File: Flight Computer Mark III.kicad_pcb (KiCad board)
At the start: 4 copper layers, 88.2 x 58.8 mm, 69 parts, among them J1 Conn_01x02, J2 USB_C_Receptacle_USB2.0_16P, Q1 PSMN075-100MSE, Q2 PSMN075-100MSE, Q3 PSMN075-100MSE, U1 CP2102N-Axx-xQFN20

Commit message: lol
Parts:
- moved 3.3VREG1 26.8 mm to (216.8, 127.4)
- moved C4 26.8 mm to (216.0, 124.3)
- moved I1 26.8 mm to (216.8, 133.4)
- moved R1 26.8 mm to (219.2, 124.9)
- moved C5 26.8 mm to (219.8, 137.1)
- moved C6 26.8 mm to (213.9, 137.1)
- moved R2 26.8 mm to (216.8, 122.6)
- moved C1 26.8 mm to (219.2, 128.1)
- moved DWNLD1 23.0 mm to (173.4, 67.0)
- moved R10 22.9 mm to (166.9, 86.3), turned to -90 degrees
- moved R13 22.5 mm to (162.0, 78.5)
- moved C11 22.4 mm to (171.0, 91.1)
- moved J2 22.4 mm to (167.8, 80.2)
- moved R11 22.4 mm to (169.1, 86.3)
- moved R18 22.4 mm to (174.1, 91.8)
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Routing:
- net MOSI_SPI0: track 8.58 -> 50.2 mm, vias 1 -> 2
- net Servo3: track 59.2 -> 22.3 mm
- net CS_SPI0: track 8.00 -> 32.6 mm, vias 0 -> 1
- net MISO_SPI0: track 21.1 -> 39.0 mm
- net TXtoURX: track 17.8 -> 30.8 mm, vias 0 -> 2
- net RXtoUTX: track 17.7 -> 28.2 mm, vias 0 -> 2
- net CLK_SPI0: track 18.7 -> 13.7 mm
- net CS_Magnetometer: track 35.5 -> 32.6 mm
- net Servo2: track 17.4 -> 19.0 mm
- net CLK_IMU: track 20.4 -> 19.0 mm
- net Servo1: track 13.2 -> 14.1 mm, vias 0 -> 1
- net GND: track 17.6 -> 16.8 mm, vias 42 -> 38

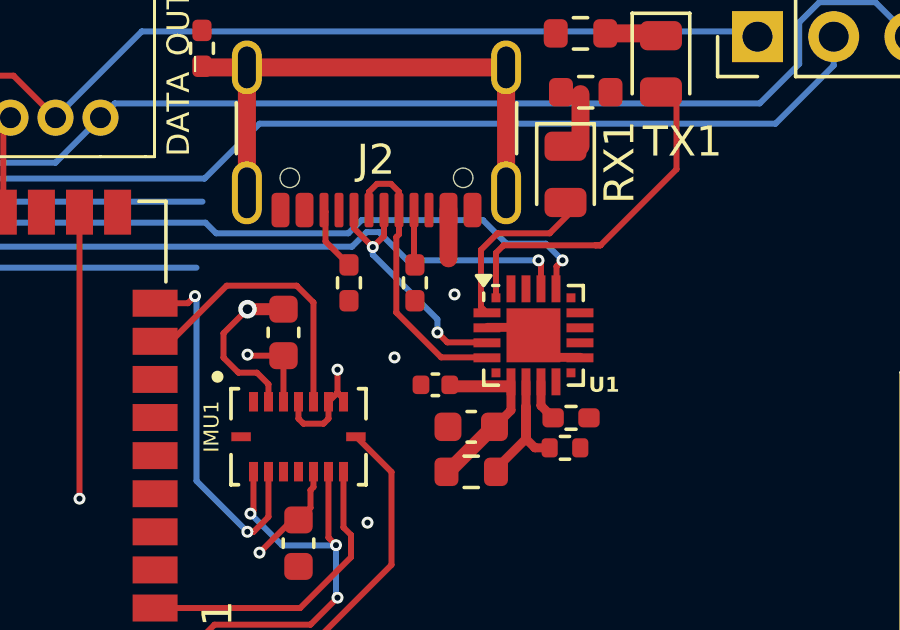
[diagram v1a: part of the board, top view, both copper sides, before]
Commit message: Added 3d models
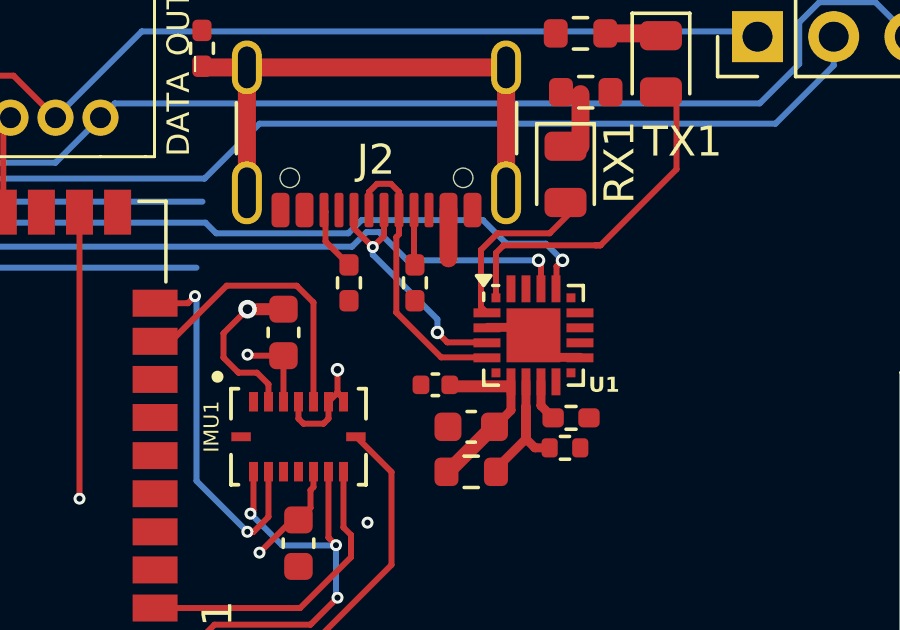
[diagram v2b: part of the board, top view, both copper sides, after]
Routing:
- net GND: vias 38 -> 36

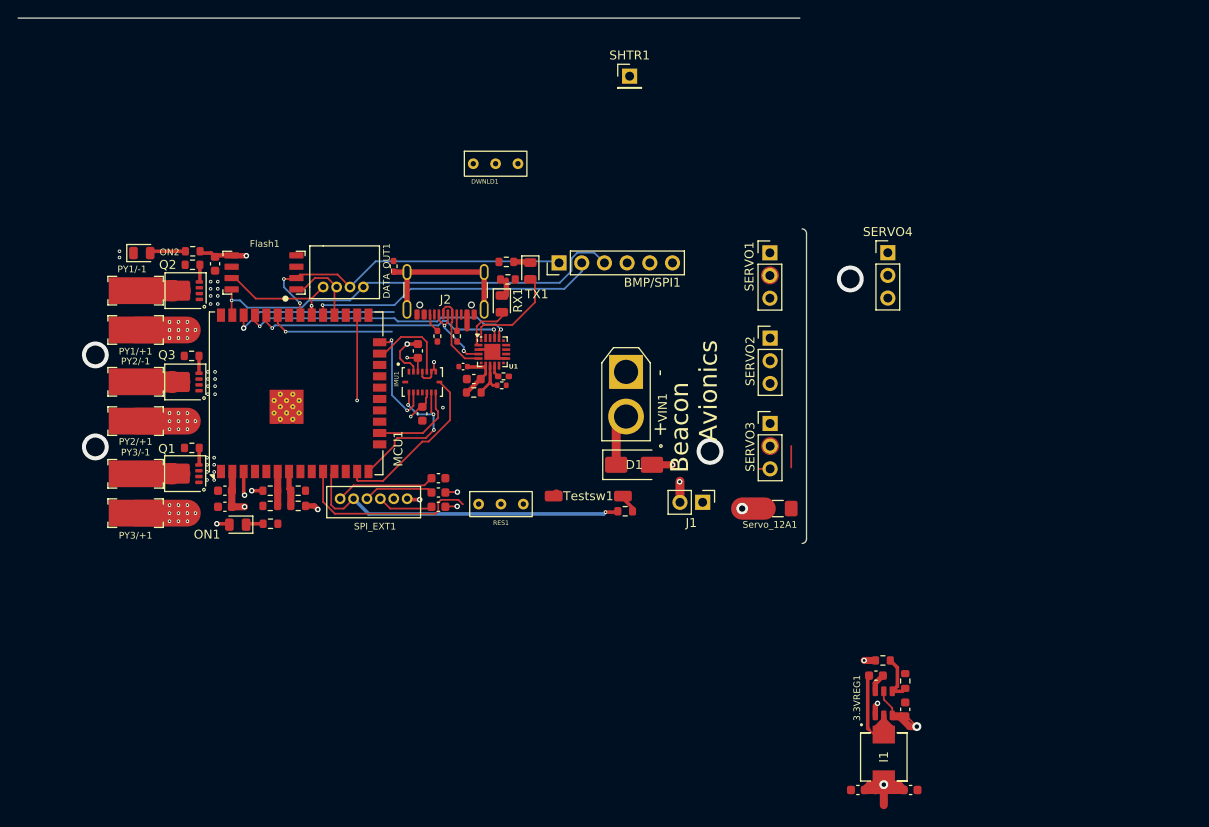
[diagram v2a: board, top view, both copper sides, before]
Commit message: Changed some via diameters, added 3D models, restructured the GND planes
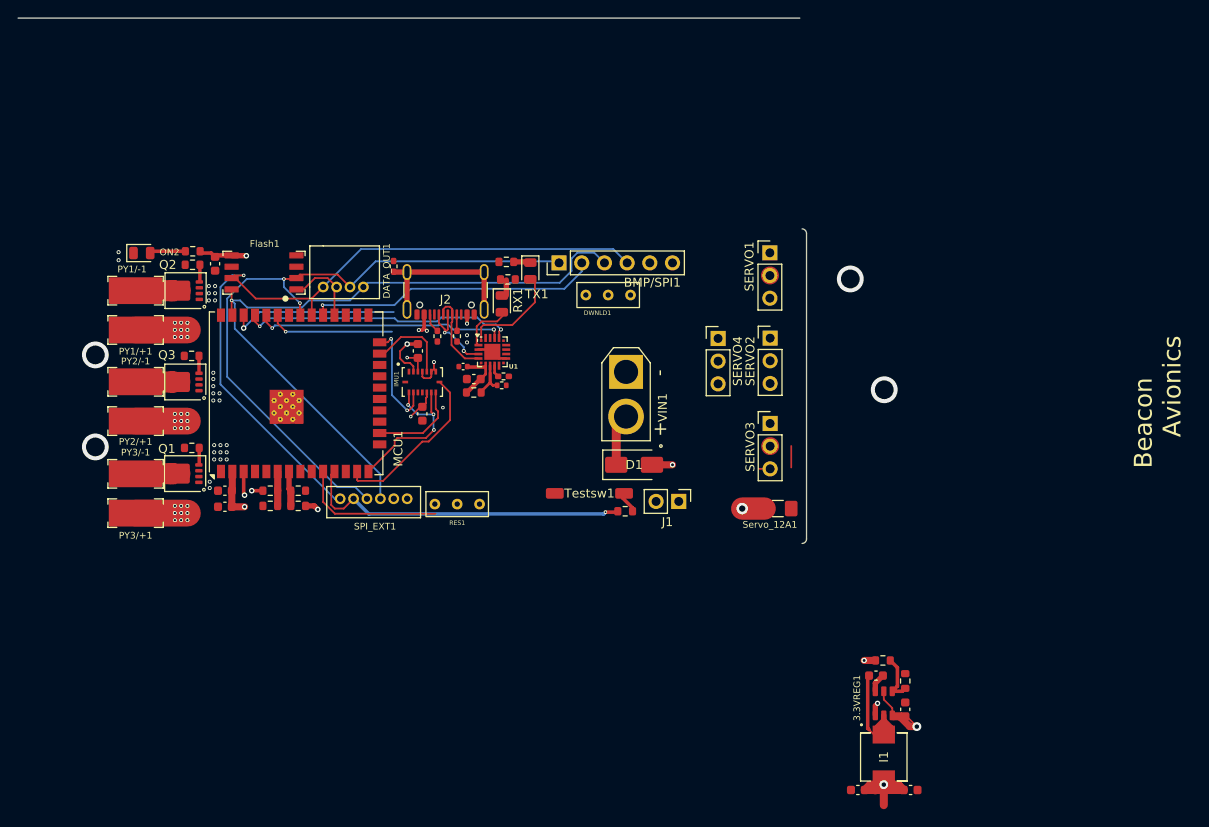
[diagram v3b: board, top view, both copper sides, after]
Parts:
- removed CLK1, MISO1, MOSI1: SolderJumper_2_Open, Capacitor_SMD:C_0603_1608Metric
- removed ON1: LED, LED_SMD:LED_0805_2012Metric
- removed R17: 400, Resistor_SMD:R_0603_1608Metric
- removed SHTR1: Conn_01x01, Connector_PinHeader_2.54mm:PinHeader_1x01_P2.54mm_Vertical
- moved SERVO4 21.3 mm to (198.3, 86.6)
- moved DWNLD1 19.4 mm to (186.0, 81.7)
- moved RES1 4.90 mm to (169.1, 105.1)
- moved J1 2.68 mm to (193.9, 104.8)
- moved Testsw1 0.32 mm to (183.9, 103.9)
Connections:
- SPI_EXT1 pad 3: MOSI_SPIEXT -> MOSI_SPI0
- SPI_EXT1 pad 4: MISO_SPIEXT -> MISO_SPI0
- SPI_EXT1 pad 6: CLK_SPIEXT -> CLK_SPI0
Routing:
- net CLK_SPI0: track 13.7 -> 84.3 mm
- net 7.4V_unfused: track 44.6 -> 91.3 mm, vias 33 -> 30
- net MISO_SPI0: track 39.0 -> 75.0 mm, vias 3 -> 2
- net CS_Magnetometer: track 32.6 -> 0.14 mm, vias 2 -> 0
- net MOSI_SPI0: track 50.2 -> 77.9 mm, vias 2 -> 1
- net CLK_SPIEXT: track 11.2 -> 0.00 mm
- net USB5V: track 10.0 -> 19.9 mm, vias 1 -> 6
- net MISO_SPIEXT: track 7.85 -> 0.00 mm
- net MOSI_SPIEXT: track 6.26 -> 0.00 mm
- net EN: track 32.6 -> 27.7 mm
- net Servo3: track 22.3 -> 17.8 mm
- net GND: track 16.8 -> 13.1 mm, vias 36 -> 34
- net Net-(ON1-K): track 1.94 -> 0.00 mm
- net D+: track 8.43 -> 9.50 mm

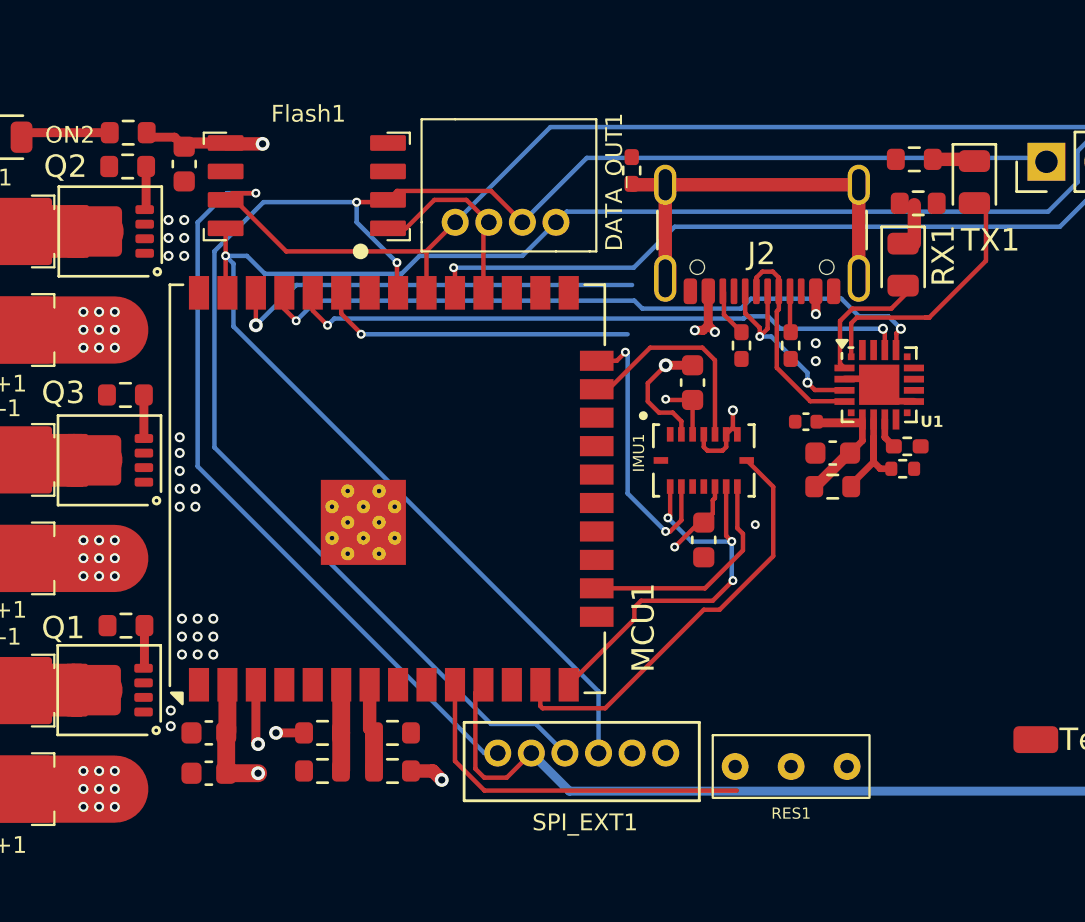
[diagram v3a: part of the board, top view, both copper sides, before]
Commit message: Added GND vias, changed some via sizes
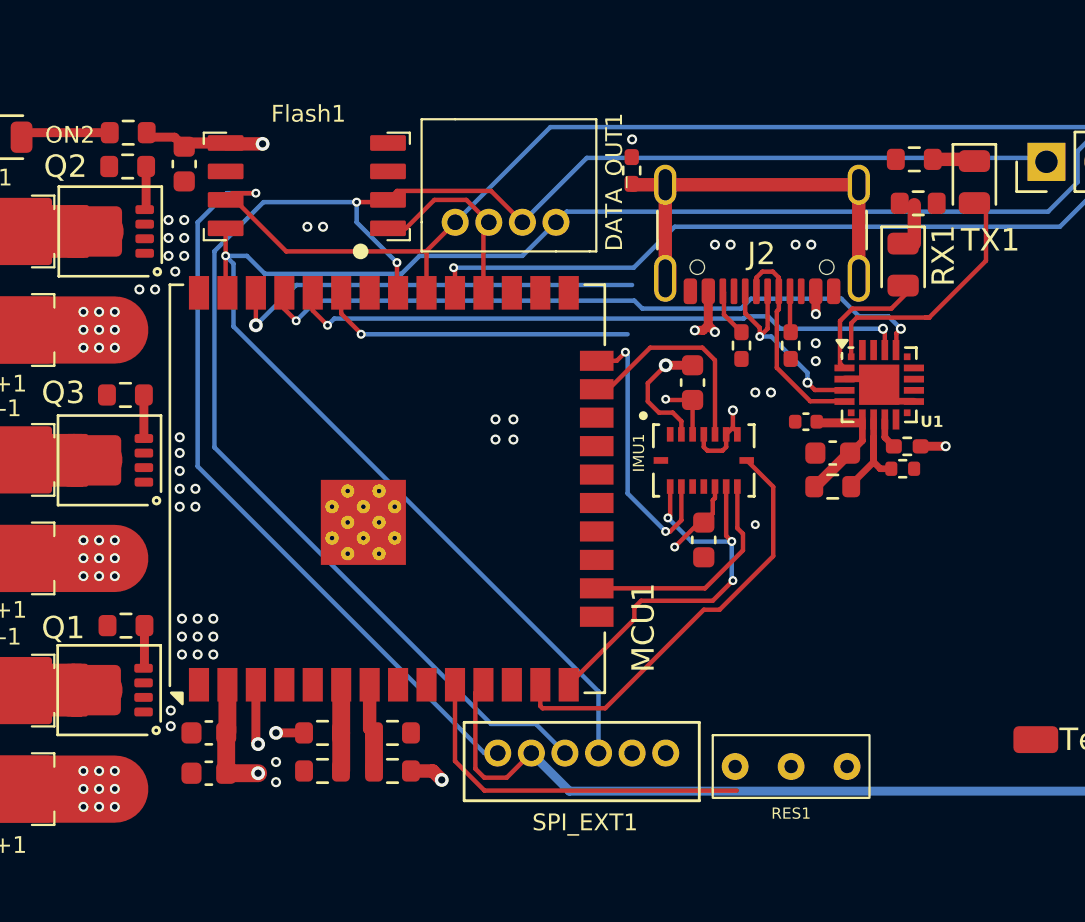
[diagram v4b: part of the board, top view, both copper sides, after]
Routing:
- net 3.3V: track 35.2 -> 36.3 mm, vias 7 -> 8
- net GND: vias 34 -> 52

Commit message: Finished Layout, TODO: DRM check
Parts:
- moved R1 57.2 mm to (168.7, 98.1), turned to 180 degrees
- moved C1 56.1 mm to (171.9, 98.1), turned to 180 degrees
- moved C5 55.5 mm to (180.9, 97.5), turned to -90 degrees
- moved R2 54.9 mm to (166.4, 100.6), turned to 90 degrees
- moved C4 53.1 mm to (168.1, 101.4), turned to -90 degrees
- moved 3.3VREG1 53.0 mm to (171.2, 100.5), turned to 180 degrees
- moved I1 51.5 mm to (177.2, 100.5), turned to 0 degrees
- moved C6 47.2 mm to (180.9, 103.4), turned to 90 degrees
- moved DWNLD1 25.3 mm to (176.4, 105.1)
- moved J1 7.91 mm to (186.0, 105.2)
- moved Servo_12A1 7.76 mm to (198.3, 101.7), turned to 90 degrees
- moved R12 6.67 mm to (183.1, 101.3), turned to -90 degrees
- moved Testsw1 5.86 mm to (184.9, 98.1), turned to 90 degrees
- moved D1 5.25 mm to (191.6, 105.2)
- moved VIN1 5.25 mm to (190.7, 94.8)
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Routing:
- net 3.3V: track 36.3 -> 201.0 mm, vias 8 -> 9
- net 7.4V_fused 12A: track 2.44 -> 82.4 mm, vias 0 -> 4
- net IO0: track 0.00 -> 72.3 mm, vias 0 -> 3
- net 7.4V_unfused: track 91.8 -> 149.9 mm, vias 30 -> 35
- net Servo2: track 19.0 -> 74.7 mm
- net USB5V: track 19.9 -> 67.7 mm, vias 6 -> 7
- net Servo1: track 14.1 -> 58.9 mm
- net Servo3: track 17.8 -> 55.0 mm
- net Mosfet1Gate: track 1.95 -> 31.4 mm, vias 0 -> 2
- net Mosfet2Gate: track 1.94 -> 21.4 mm
- net Mosfet3Gate: track 2.45 -> 15.6 mm
- net Net-(U1-VBUS): track 5.51 -> 4.41 mm
- net CLK_SPI0: track 84.3 -> 85.3 mm
- net TXtoURX: track 30.8 -> 31.6 mm
- net MISO_SPI0: track 75.0 -> 75.7 mm
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- added copper zone on B.Cu, net GND
- added copper zone on F.Cu, net GND
- added copper zone on In1.Cu, net GND
- added copper zone on In2.Cu, net GND
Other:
- board size 88.2 x 58.8 mm -> 79.7 x 33.2 mm

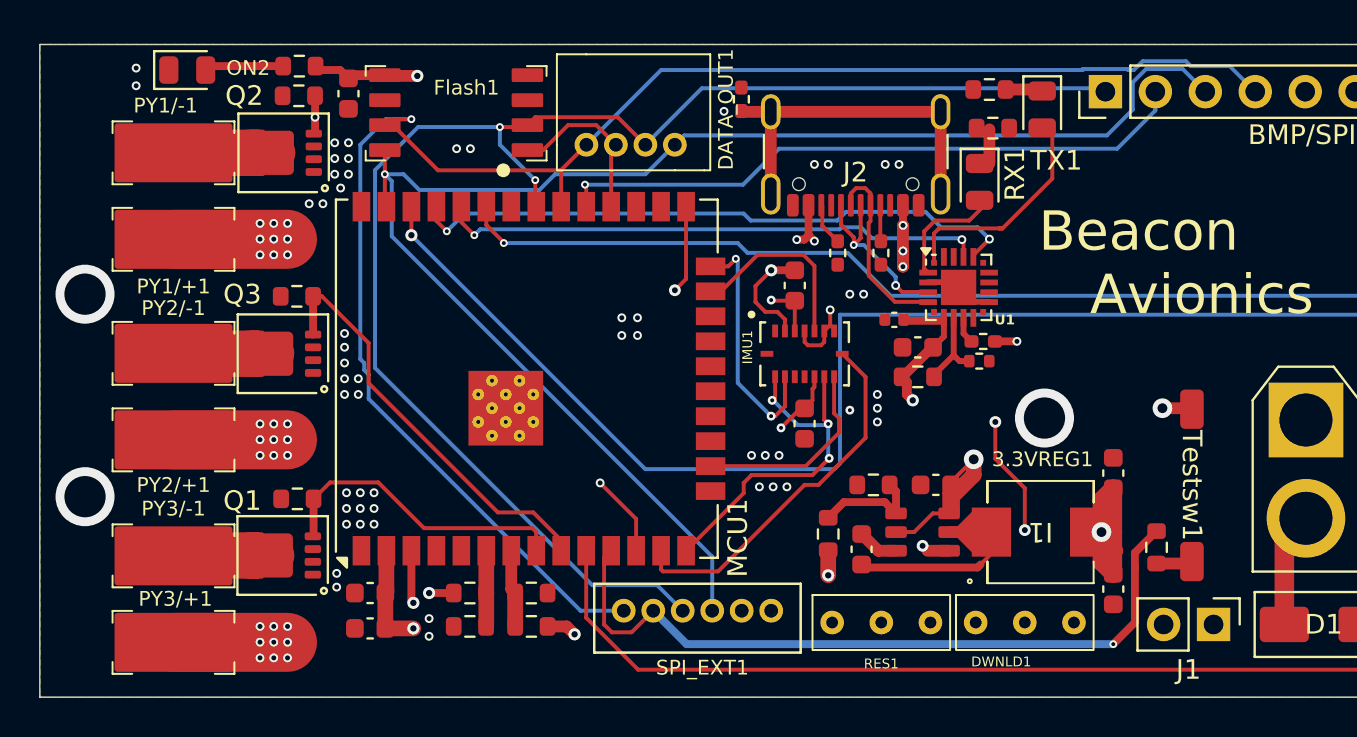
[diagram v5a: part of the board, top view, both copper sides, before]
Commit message: changed via diamters according to DRC requirements
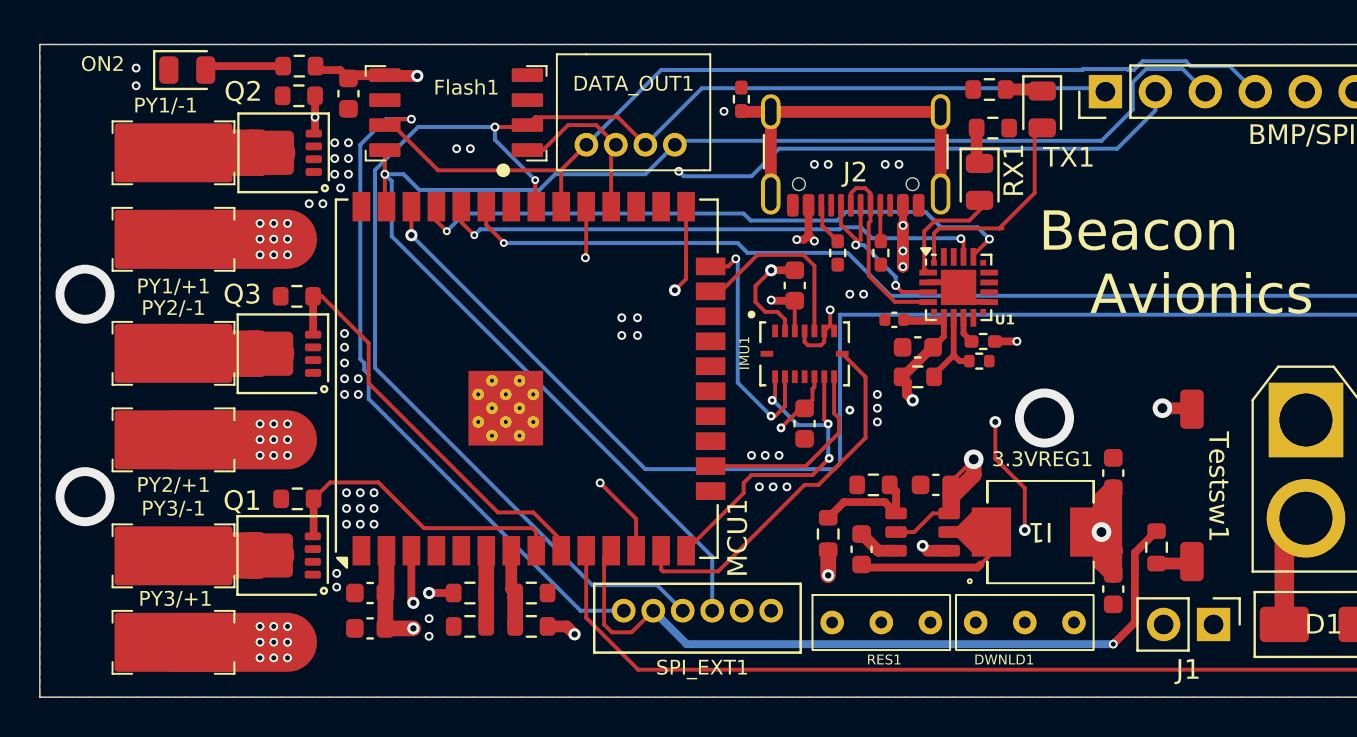
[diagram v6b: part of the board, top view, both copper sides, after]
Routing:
- net CS_SPI0: track 32.6 -> 35.9 mm, vias 1 -> 2
